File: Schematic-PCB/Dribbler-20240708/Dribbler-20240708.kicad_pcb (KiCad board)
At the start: 2 copper layers, 28.5 x 25 mm, 8 parts, among them J2 Conn_01x02_Pin, J3 Conn_01x02_Pin, J4 Conn_01x04_Pin

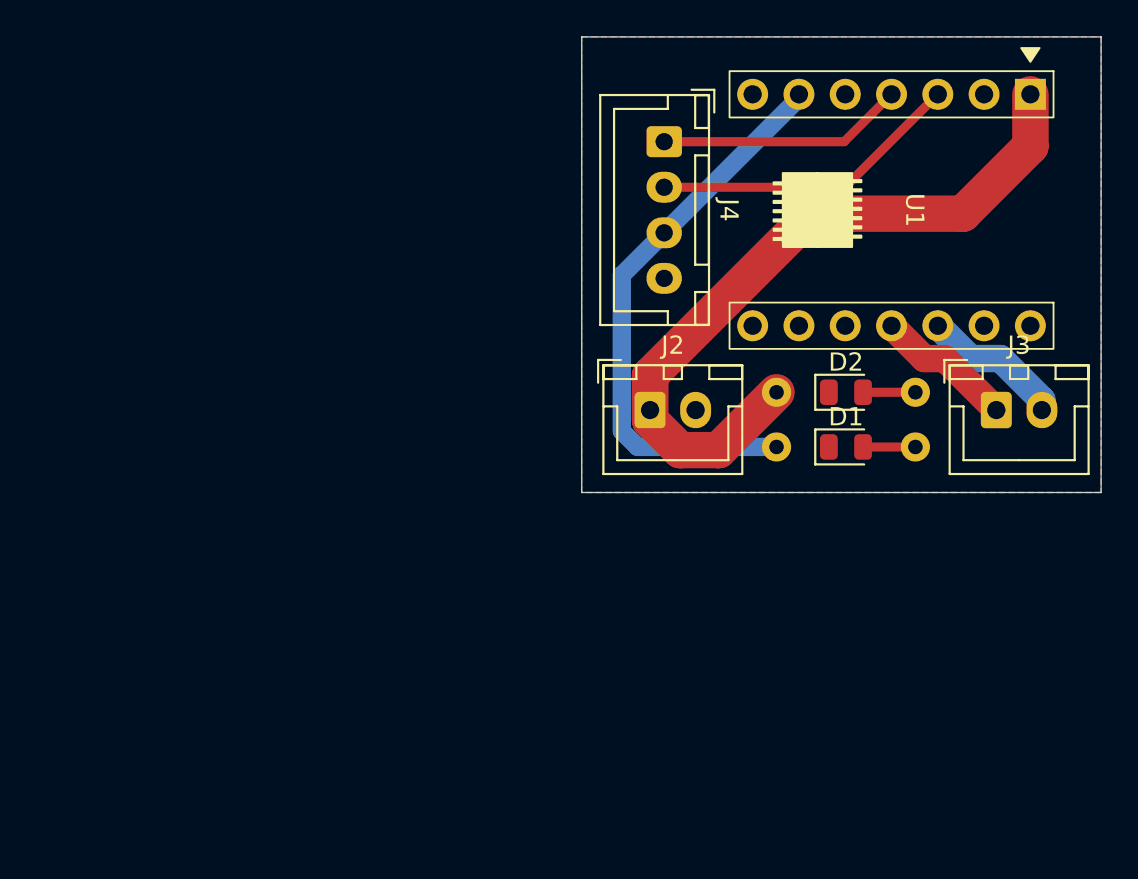
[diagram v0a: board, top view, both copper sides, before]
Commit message: ドリブラー基板の外形とかを仮完成させた
めちゃミニミニ基板になったよ
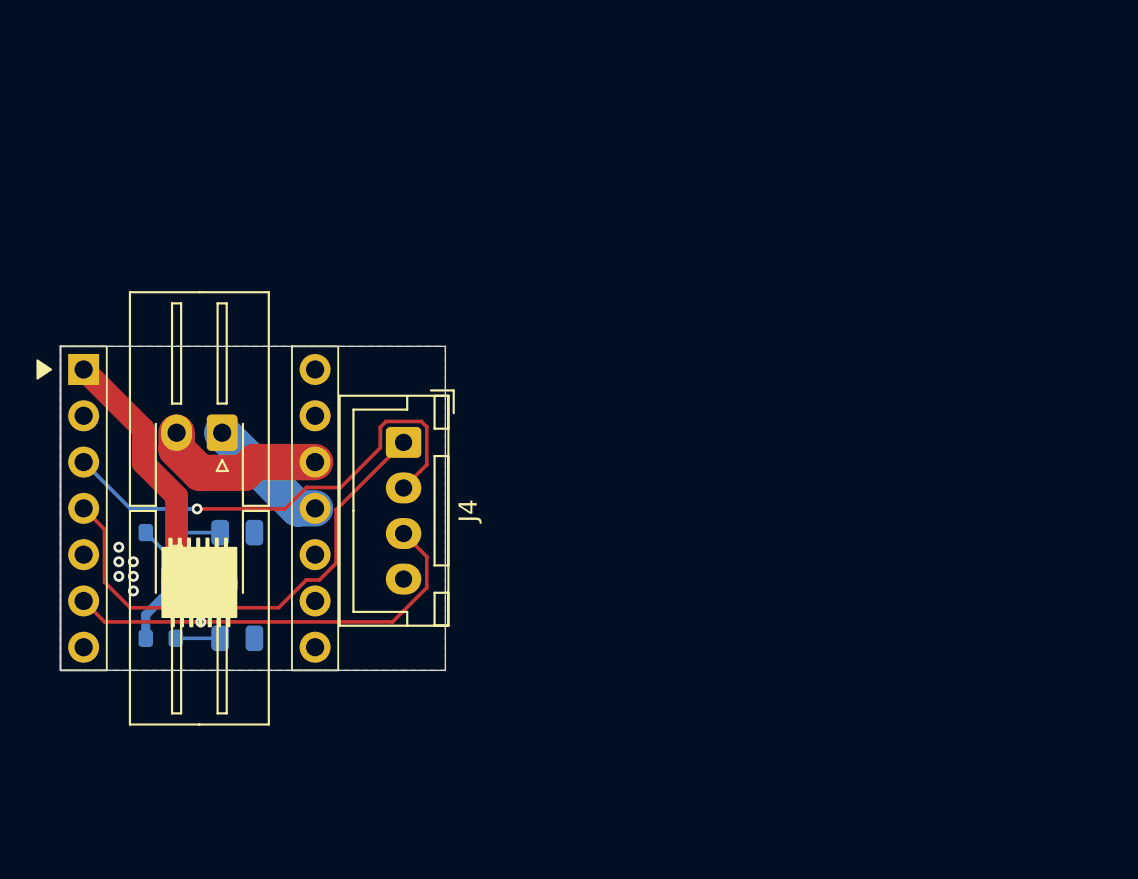
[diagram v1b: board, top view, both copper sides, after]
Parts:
- D1, D2: moved to B.Cu
- J2, J3: footprint Connector_JST:JST_XH_B2B-XH-A_1x02_P2.50mm_Vertical -> Connector_JST:JST_XH_S2B-XH-A-1_1x02_P2.50mm_Horizontal
- R1, R2: footprint Resistor_THT:R_Axial_DIN0207_L6.3mm_D2.5mm_P7.62mm_Horizontal -> Resistor_SMD:R_0603_1608Metric
- moved R2 43.6 mm to (94.4, 110.0)
- moved J3 42.5 mm to (97.8, 98.7), turned to 180 degrees
- moved R1 41.7 mm to (94.4, 104.2)
- moved U1 41.4 mm to (96.5, 102.9), turned to 0 degrees
- moved D2 36.0 mm to (98.6, 110.0), turned to 180 degrees
- moved D1 33.7 mm to (98.6, 104.2), turned to 180 degrees
- moved J2 27.7 mm to (95.3, 107.0)
- moved J4 21.8 mm to (107.7, 99.2)
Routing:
- net VCC: track 42.2 -> 17.6 mm
- net PH: track 13.6 -> 27.0 mm
- net EN: track 17.1 -> 26.5 mm, vias 0 -> 1
- net OUT1: track 7.95 -> 9.29 mm
- net +3.3V: track 31.4 -> 30.5 mm, vias 0 -> 1
- net OUT2: track 7.67 -> 6.82 mm
- net GND: vias 0 -> 6
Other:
- board size 28.5 x 25 mm -> 21.1 x 17.8 mm

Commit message: ドリブラー基板のPCBを完成させた
設計通りの基板外形でやったよ
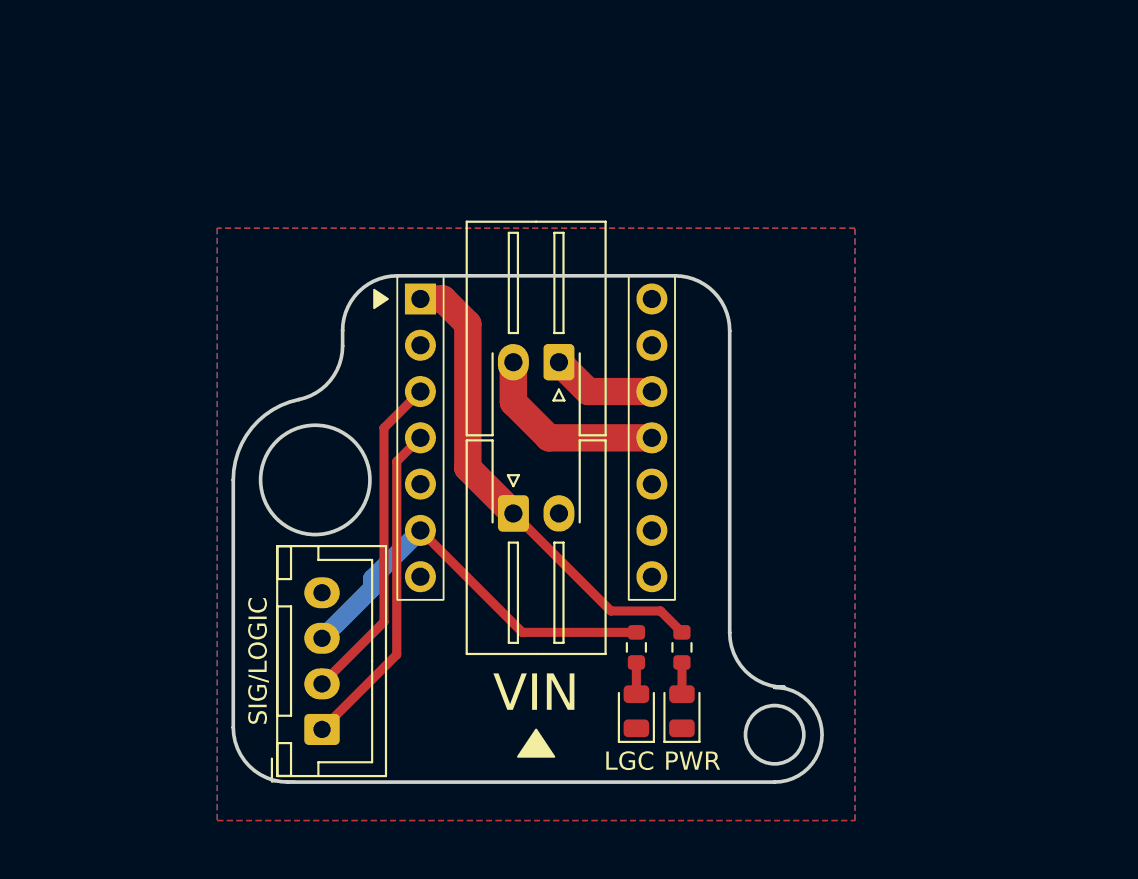
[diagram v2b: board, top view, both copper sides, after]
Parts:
- removed D1: Signal, LED_SMD:LED_0805_2012Metric
- removed D2: Power, LED_SMD:LED_0805_2012Metric
- removed J2: Conn_01x02_Pin, Connector_JST:JST_XH_S2B-XH-A-1_1x02_P2.50mm_Horizontal
- removed J4: Conn_01x04_Pin, Connector_JST:JST_XH_B4B-XH-A_1x04_P2.50mm_Vertical
- added LGC: Signal, LED_SMD:LED_0805_2012Metric, F.Cu at (120.5, 114.0)
- added PWR: Power, LED_SMD:LED_0805_2012Metric, F.Cu at (123.0, 114.0)
- added SIG/LOGIC: Conn_01x04_Pin, Connector_JST:JST_XH_B4B-XH-A_1x04_P2.50mm_Vertical, F.Cu at (103.2, 115.0)
- added VIN: Conn_01x02_Pin, Connector_JST:JST_XH_S2B-XH-A-1_1x02_P2.50mm_Horizontal, F.Cu at (113.8, 103.2)
- R1, R2: moved to F.Cu
- moved R2 28.6 mm to (123.0, 110.5), turned to 90 degrees
- moved R1 26.8 mm to (120.5, 110.5), turned to 90 degrees
- moved J3 18.9 mm to (116.2, 94.8)
- moved U1 18.9 mm to (115.0, 99.0)
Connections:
- J3 pad 1: OUT2 -> OUT1
- J3 pad 2: OUT1 -> OUT2
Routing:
- net VCC: track 17.6 -> 26.6 mm
- net PH: track 27.0 -> 18.2 mm
- net EN: track 26.5 -> 18.3 mm, vias 1 -> 0
- net +3.3V: track 30.5 -> 22.3 mm, vias 1 -> 0
- net OUT2: track 6.82 -> 10.6 mm
- net OUT1: track 9.29 -> 5.77 mm
- net Net-(D2-A): track 2.44 -> 1.74 mm
- net Net-(D1-A): track 2.44 -> 1.74 mm
- net GND: vias 6 -> 0
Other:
- board size 21.1 x 17.8 mm -> 32.3 x 27.8 mm

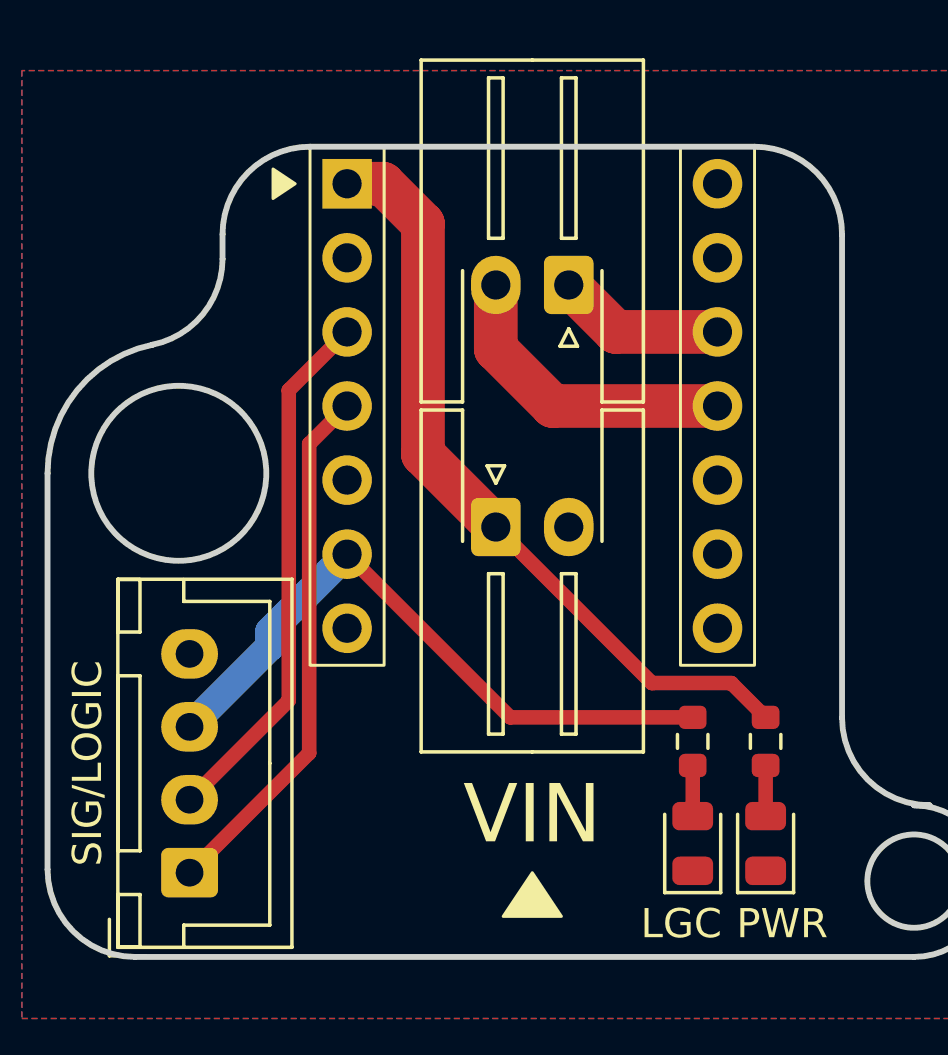
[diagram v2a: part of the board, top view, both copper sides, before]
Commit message: ドリブラー基板の発注用ファイルを作成した
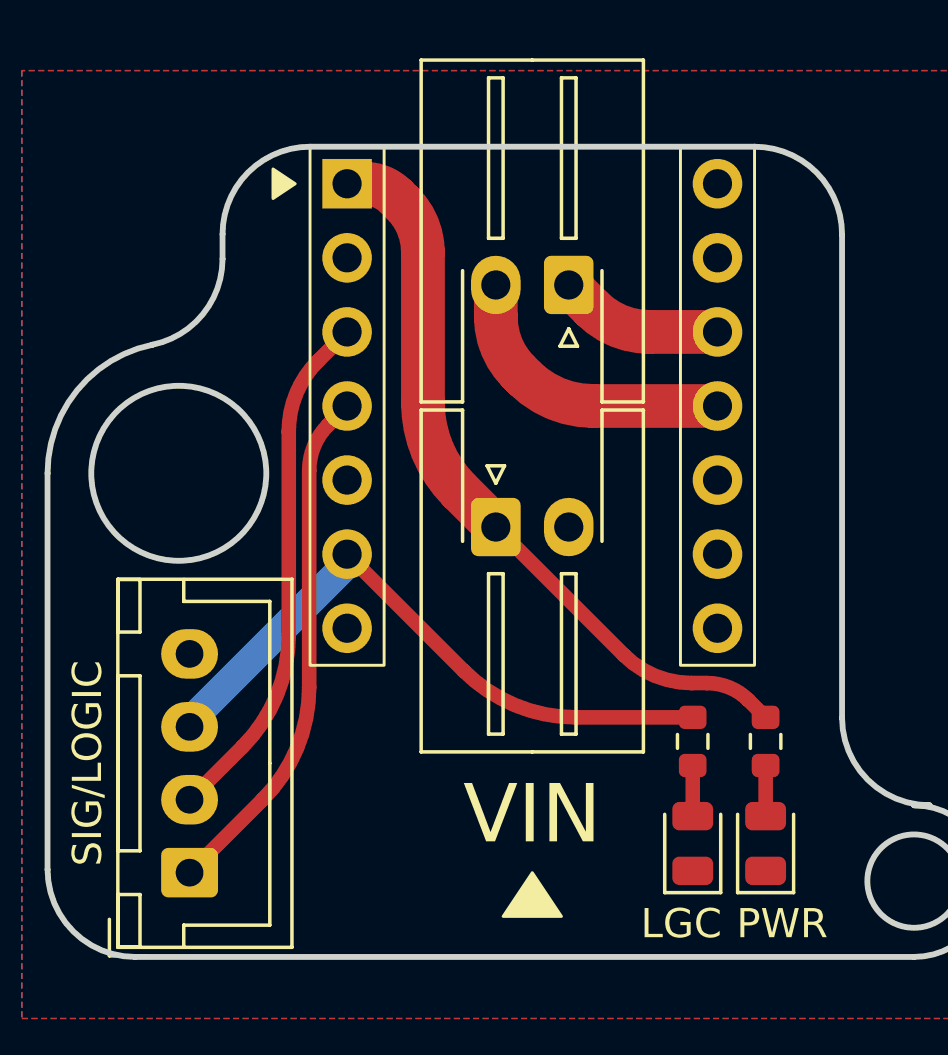
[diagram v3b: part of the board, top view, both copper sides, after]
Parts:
- R1, R2: value R_Small -> 330
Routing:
- net VCC: track 26.6 -> 25.9 mm
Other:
- board text added: "Dribbler #001"

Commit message: ドリブラーのプログラムを追加した
なんでコンパイル通らないのかぁぁぁぁぁ
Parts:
- added REF**: MountingHole_6.4mm_M6, MountingHole:MountingHole_6.4mm_M6, F.Cu at (104.0, 102.5)
- moved J3 1.64 mm to (117.4, 96.0)
- moved LGC 1.64 mm to (121.6, 115.2)
- moved PWR 1.64 mm to (124.1, 115.2)
- moved R1 1.64 mm to (121.6, 111.7)
- moved R2 1.64 mm to (124.1, 111.7)
- moved SIG/LOGIC 1.64 mm to (104.4, 116.2)
- moved U1 1.64 mm to (116.1, 100.2)
- moved VIN 1.64 mm to (114.9, 104.3)
